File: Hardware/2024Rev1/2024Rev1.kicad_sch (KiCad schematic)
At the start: 84 parts, among them J7 RJ45_LED_Shielded, Q2 BSS138, Q3 BSS138, Q5 BSS138, Q6 SPD30P06PGBTMA1, Q7 BSS138, U2 Opamp_Dual, U3 Teensy4.1_DEV-16771, U4 Opamp_Dual, U5 Opamp_Dual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

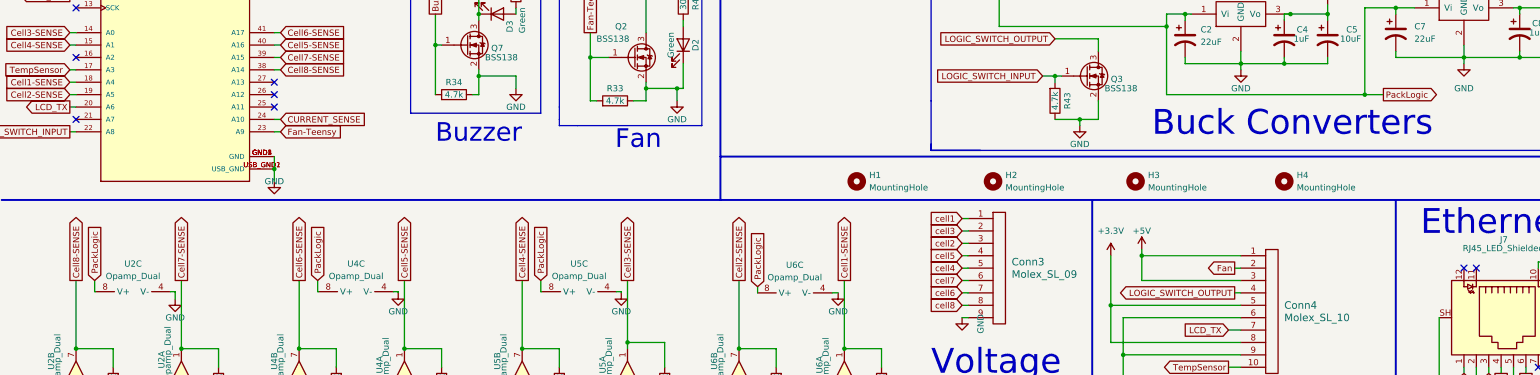
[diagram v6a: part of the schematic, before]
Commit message: redid ethernet traces
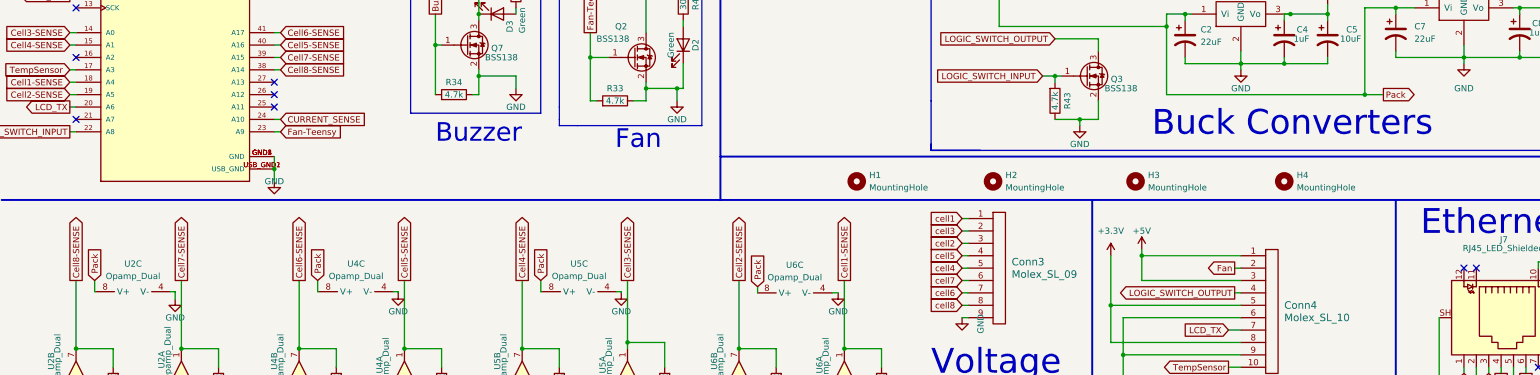
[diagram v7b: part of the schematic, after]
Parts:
- Q6: footprint Package_TO_SOT_SMD:TO-263-7_TabPin4 -> Package_TO_SOT_SMD:TO-263-7_TabPin8
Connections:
- net PackLogic renamed Pack
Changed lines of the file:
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@@
     )
   )
-  (global_label "PackLogic" (shape input) (at 123.19 135.89 90) (fields_autoplaced)
-    (effects (font (size 1.27 1.27)) (justify left))
-    (property "Intersheetrefs" "${INTERSHEET_REFS}" (at 123.1106 123.9217 90)
+  (global_label "Pack" (shape input) (at 123.19 135.89 90) (fields_autoplaced)
+    (effects (font (size 1.27 1.27)) (justify left))
+    (property "Intersheetrefs" "${INTERSHEET_REFS}" (at 123.19 128.3691 90)
       (effects (font (size 1.27 1.27)) (justify left) hide)
     )
@@
     )
   )
-  (global_label "PackLogic" (shape input) (at 77.47 135.89 90) (fields_autoplaced)
-    (effects (font (size 1.27 1.27)) (justify left))
-    (property "Intersheetrefs" "${INTERSHEET_REFS}" (at 77.3906 123.9217 90)
+  (global_label "Pack" (shape input) (at 77.47 135.89 90) (fields_autoplaced)
+    (effects (font (size 1.27 1.27)) (justify left))
+    (property "Intersheetrefs" "${INTERSHEET_REFS}" (at 77.47 128.3691 90)
       (effects (font (size 1.27 1.27)) (justify left) hide)
     )
@@
     )
   )
-  (global_label "PackLogic" (shape output) (at 295.91 97.79 0) (fields_autoplaced)
-    (effects (font (size 1.27 1.27)) (justify left))
-    (property "Intersheetrefs" "${INTERSHEET_REFS}" (at 307.8783 97.7106 0)
+  (global_label "Pack" (shape output) (at 295.91 97.79 0) (fields_autoplaced)
+    (effects (font (size 1.27 1.27)) (justify left))
+    (property "Intersheetrefs" "${INTERSHEET_REFS}" (at 303.4309 97.79 0)
       (effects (font (size 1.27 1.27)) (justify left) hide)
     )
@@
     )
   )
-  (global_label "PackLogic" (shape input) (at 31.75 135.89 90) (fields_autoplaced)
-    (effects (font (size 1.27 1.27)) (justify left))
-    (property "Intersheetrefs" "${INTERSHEET_REFS}" (at 31.6706 123.9217 90)
+  (global_label "Pack" (shape input) (at 31.75 135.89 90) (fields_autoplaced)
+    (effects (font (size 1.27 1.27)) (justify left))
+    (property "Intersheetrefs" "${INTERSHEET_REFS}" (at 31.75 128.3691 90)
       (effects (font (size 1.27 1.27)) (justify left) hide)
     )
@@
     )
   )
-  (global_label "PackLogic" (shape input) (at 167.64 137.16 90) (fields_autoplaced)
-    (effects (font (size 1.27 1.27)) (justify left))
-    (property "Intersheetrefs" "${INTERSHEET_REFS}" (at 167.5606 125.1917 90)
+  (global_label "Pack" (shape input) (at 167.64 137.16 90) (fields_autoplaced)
+    (effects (font (size 1.27 1.27)) (justify left))
+    (property "Intersheetrefs" "${INTERSHEET_REFS}" (at 167.64 129.6391 90)
       (effects (font (size 1.27 1.27)) (justify left) hide)
     )
@@
       (effects (font (size 1.27 1.27)) (justify left))
     )
-    (property "Footprint" "Package_TO_SOT_SMD:TO-263-7_TabPin4" (at 265.43 26.035 0)
+    (property "Footprint" "Package_TO_SOT_SMD:TO-263-7_TabPin8" (at 265.43 26.035 0)
       (effects (font (size 1.27 1.27) italic) (justify left) hide)
     )

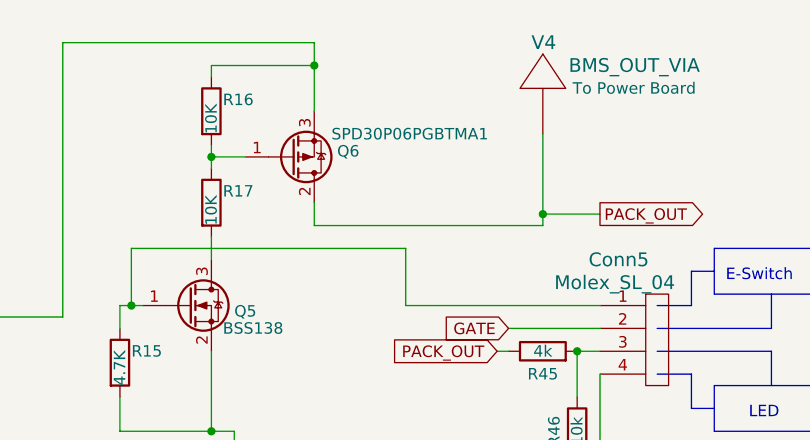
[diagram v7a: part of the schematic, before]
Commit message: redid zones and added in vias for zones
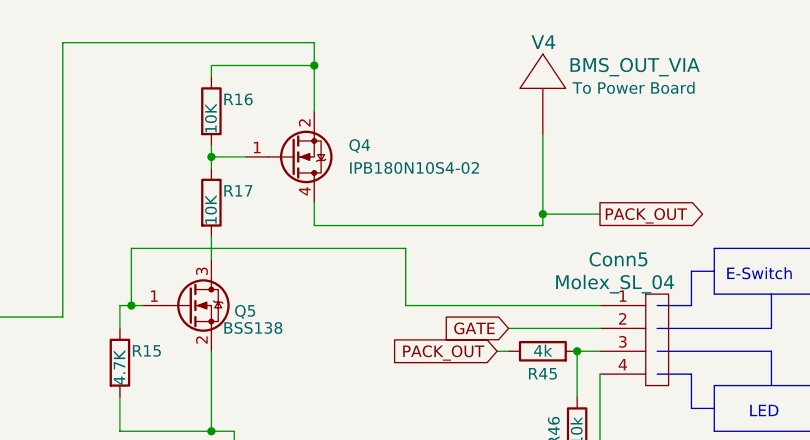
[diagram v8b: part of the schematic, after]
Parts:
- removed Q6: SPD30P06PGBTMA1, Package_TO_SOT_SMD:TO-263-7_TabPin8, symbol Transistor_FET:QM6015D
- added Q4: IPB180N10S4-02, Package_TO_SOT_SMD:TO-263-6, symbol Transistor_FET:IPB180N10S4-02
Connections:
- net PACK_OUT: now also Q4.4 (D)
- net Pack: now also Q4.2 (S), Q4.3 (S), Q4.5 (S), Q4.6 (S), Q4.7 (S)
- net at R16.2, R17.1: now also Q4.1 (G)
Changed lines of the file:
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@@
-    )
-  )
-  (symbol (lib_id "Transistor_FET:QM6015D") (at 260.35 27.94 0) (mirror x) (unit 1)
-    (in_bom yes) (on_board yes) (dnp no)
-    (property "Reference" "Q6" (at 265.43 27.305 0)
-      (effects (font (size 1.27 1.27)) (justify left))
-    )
-    (property "Value" "SPD30P06PGBTMA1" (at 264.795 25.4 0)
-      (effects (font (size 1.27 1.27)) (justify left))
-    )
-    (property "Footprint" "Package_TO_SOT_SMD:TO-263-7_TabPin8" (at 265.43 26.035 0)
-      (effects (font (size 1.27 1.27) italic) (justify left) hide)
-    )
-    (property "Datasheet" "https://www.infineon.com/dgdl/SPD30P06P_Rev.2.3.pdf?folderId=db3a30431ed1d7b2011f4042f2ff4ec5&fileId=db3a30431ed1d7b2011f404fbc7e4ef4" (at 260.35 27.94 90)
-      (effects (font (size 1.27 1.27)) (justify left) hide)
-    )
-    (pin "1")
-    (pin "2")
-    (pin "3")
-    (instances
-      (project "2024Rev1"
-        (path "/62a5013b-27bd-4648-9844-b43a50a9ebdc"
-          (reference "Q6") (unit 1)
-        )
-      )
-      (project "PowerBoard_2024"
-        (path "/8ad22d76-a558-4ba1-aeeb-dc7eabdc9e9b"
-          (reference "Q6") (unit 1)
-        )
-      )
     )
   )
@@
         )
       )
+    )
+  )
+  (symbol (lib_id "Transistor_FET:IPB180N10S4-02") (at 260.35 27.94 0) (mirror x) (unit 1)
+    (in_bom yes) (on_board yes) (dnp no)
+    (property "Reference" "Q4" (at 266.7 26.67 0)
+      (effects (font (size 1.27 1.27)) (justify left))
+    )
+    (property "Value" "IPB180N10S4-02" (at 266.7 29.21 0)
+      (effects (font (size 1.27 1.27)) (justify left))
+    )
+    (property "Footprint" "Package_TO_SOT_SMD:TO-263-6" (at 265.43 26.035 0)
+      (effects (font (size 1.27 1.27) italic) (justify left) hide)
+    )
+    (property "Datasheet" "https://www.infineon.com/dgdl/Infineon-IPB180N10S4_02-DS-v01_00-en.pdf?fileId=db3a30433d1d0bbe013d2129cf8a2f88" (at 260.35 27.94 90)
+      (effects (font (size 1.27 1.27)) (justify left) hide)
+    )
+    (pin "1")
+    (pin "2")
+    (pin "3")
+    (pin "4")
+    (pin "5")
+    (pin "6")
+    (pin "7")
+    (instances
+      (project "2024Rev1"
+        (path "/62a5013b-27bd-4648-9844-b43a50a9ebdc"
+          (reference "Q4") (unit 1)
+        )
+      )
